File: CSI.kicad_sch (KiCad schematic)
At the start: 33 parts, among them U6 MAX9295A, Y1 Resonator_25MHz_ABM8G

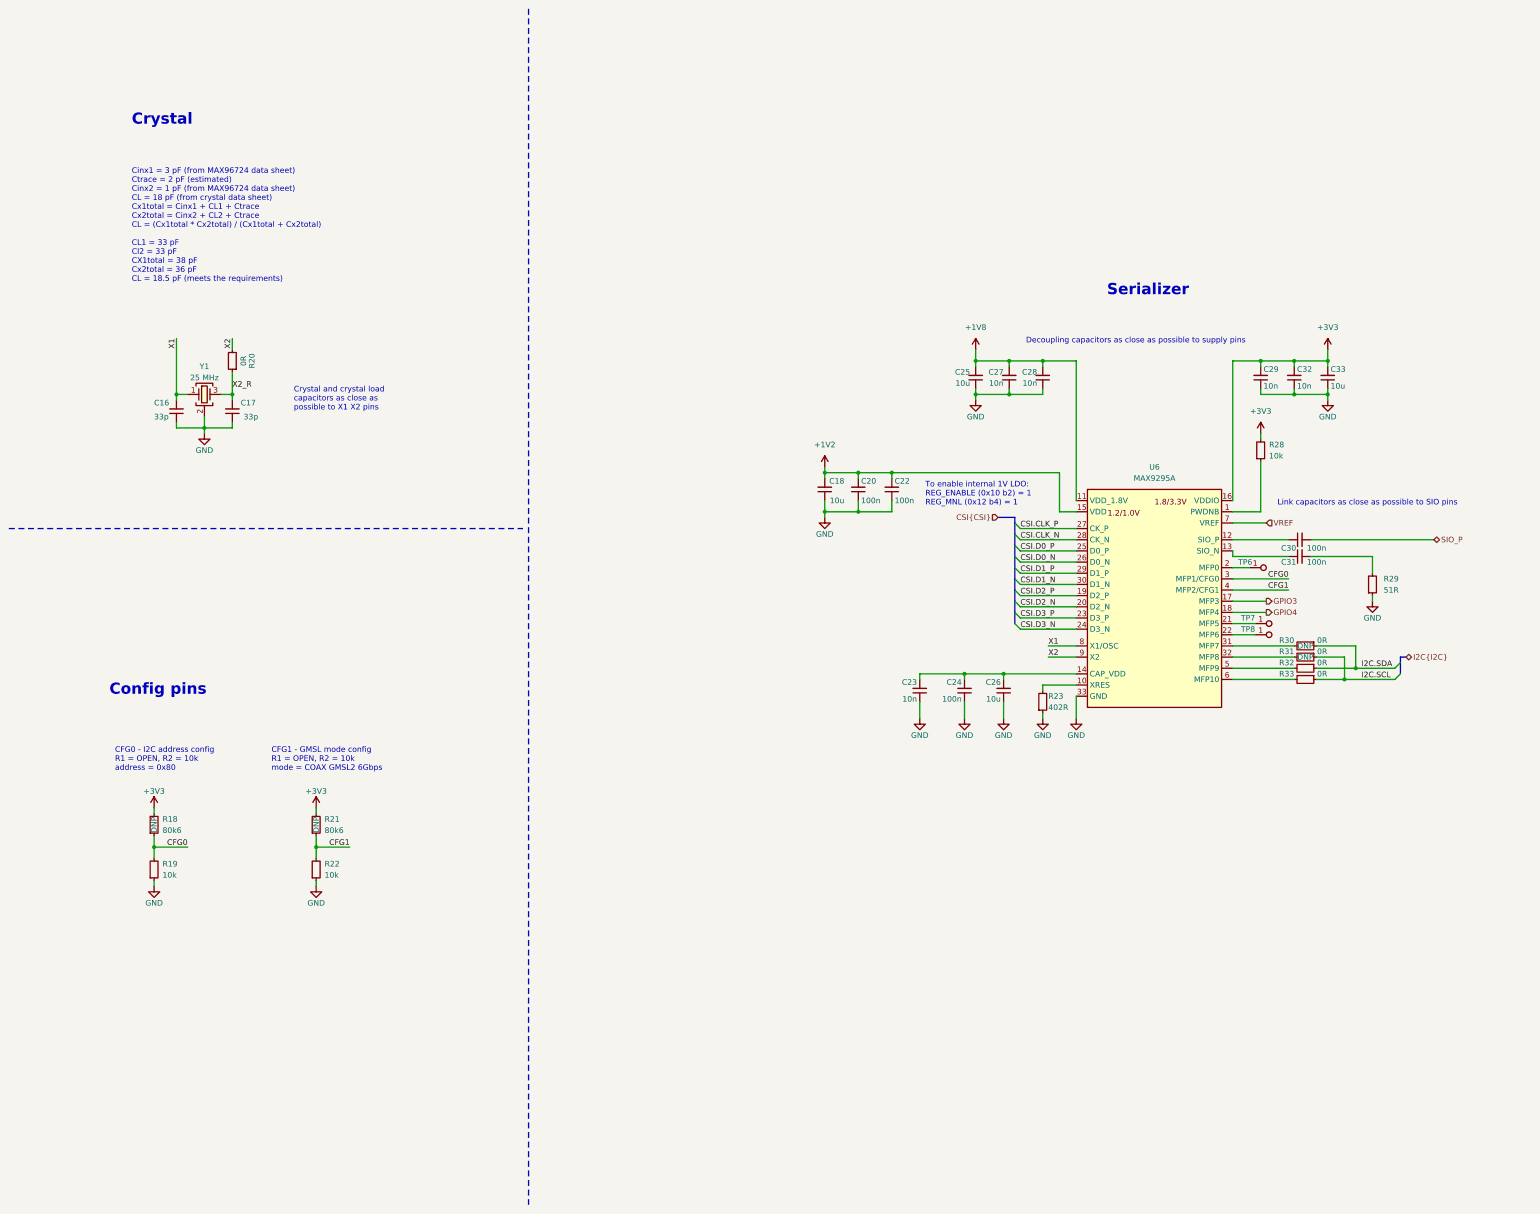
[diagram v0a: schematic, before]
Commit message: [#66847] Make schematic hierarchical
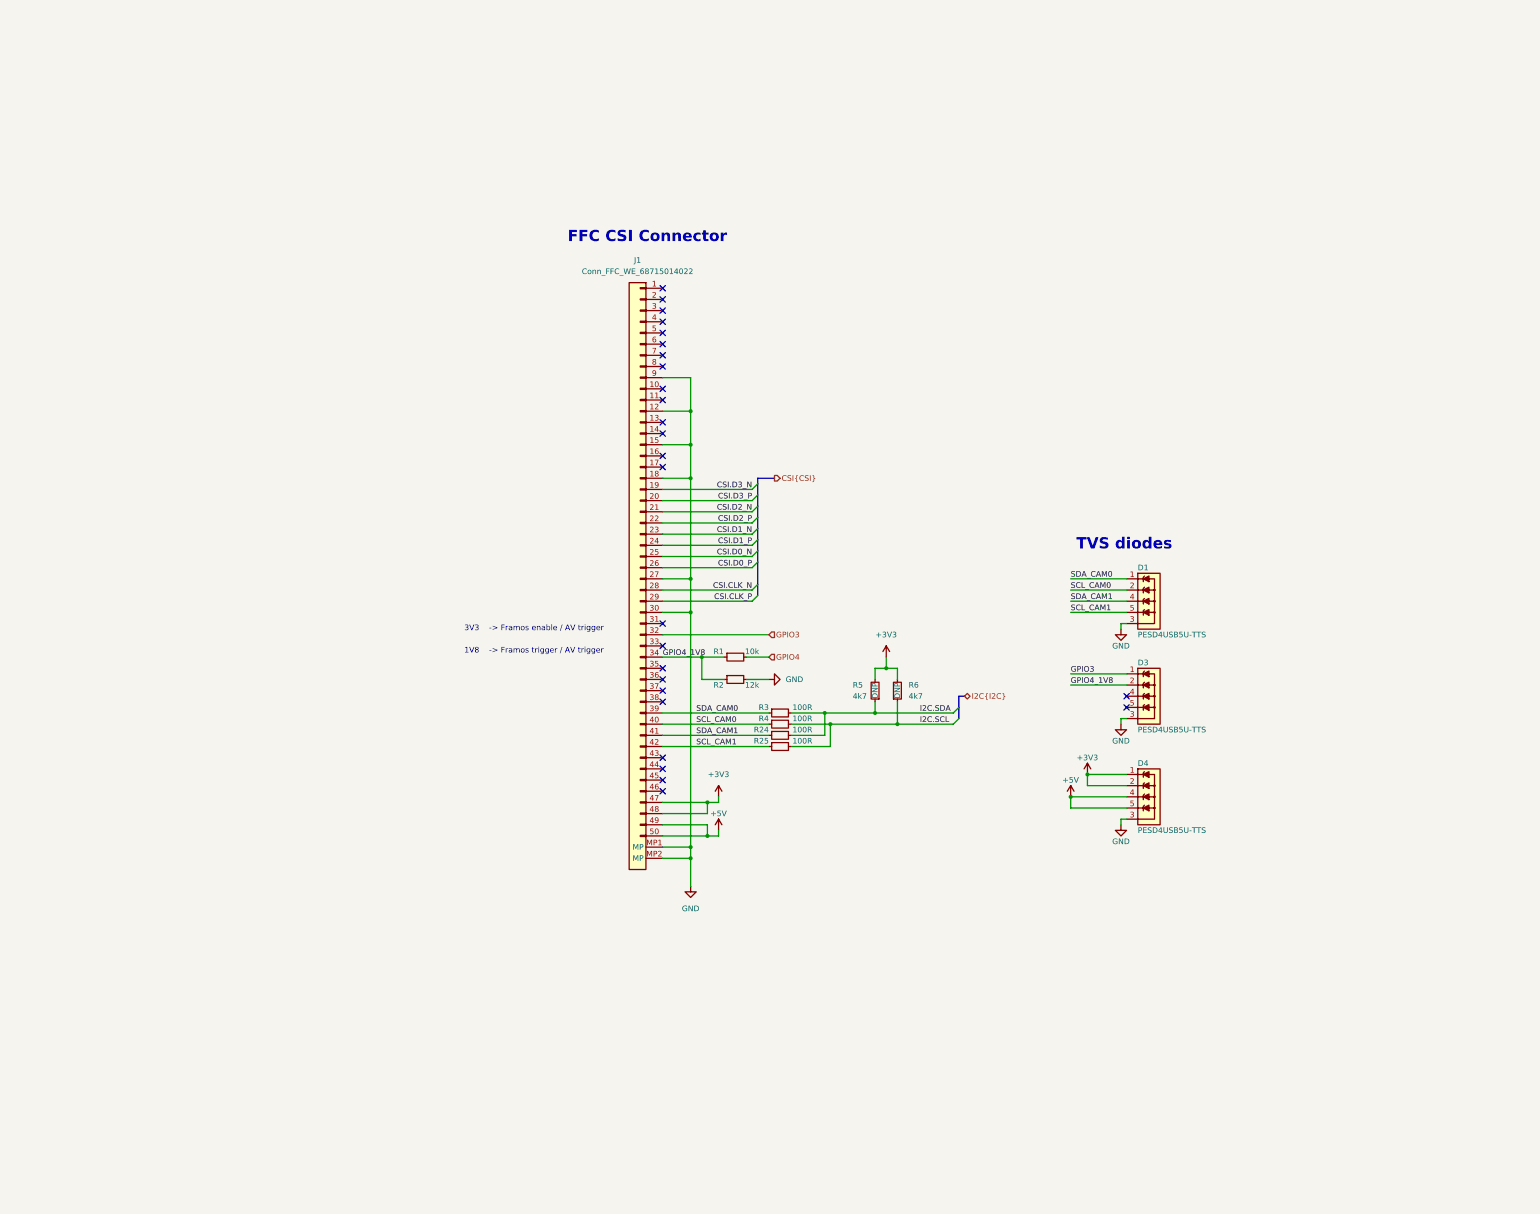
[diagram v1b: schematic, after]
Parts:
- removed C16, C17: C_33p_0402, antmicro-footprints:C_0402_1005Metric, symbol antmicroCapacitors0402:C_33p_0402
- removed C18, C25, C26, C33: C_10u_0402, antmicro-footprints:C_0402_1005Metric, symbol antmicroCapacitors0402:C_10u_0402
- removed C20, C22, C24, C30, C31: C_100n_0402, antmicro-footprints:C_0402_1005Metric, symbol antmicroCapacitors0402:C_100n_0402
- removed C23, C27, C28, C29, C32: C_10n_0402, antmicro-footprints:C_0402_1005Metric, symbol antmicroCapacitors0402:C_10n_0402
- removed R18, R21: R_80k6_0402, antmicro-footprints:R_0402_1005Metric, symbol antmicroResistors0402:R_80k6_0402
- removed R19, R22, R28: R_10k_0402, antmicro-footprints:R_0402_1005Metric, symbol antmicroResistors0402:R_10k_0402
- removed R20, R30, R31, R32, R33: R_0R_0402, antmicro-footprints:R_0402_1005Metric, symbol antmicroResistors0402:R_0R_0402
- removed R23: R_402R_0402, antmicro-footprints:R_0402_1005Metric, symbol antmicroResistors0402:R_402R_0402
- removed R29: R_51R_0402, antmicro-footprints:R_0402_1005Metric, symbol antmicroResistors0402:R_51R_0402
- removed TP6, TP7, TP8: TP_1.5mm_SMD, antmicro-footprints:TP_SMD_1.5mm, symbol antmicroTestPoints:TP_1.5mm_SMD
- removed U6: MAX9295A, antmicro-footprints:QFN-32-1EP_5x5mm, symbol antmicroInterfaceControllers:MAX9295A
- removed Y1: Resonator_25MHz_ABM8G, antmicro-footprints:Resonator_SMD_Abracon_ABM8G_3.2x2.5mm, symbol antmicroResonators:Resonator_25MHz_ABM8G
- added D1, D3, D4: PESD4USB5U-TTS, antmicro-footprints:DFN-10_2.5x1mm, symbol antmicroTVSDiodes:PESD4USB5U-TTS
- added J1: Conn_FFC_WE_68715014022, antmicro-footprints:Conn_FFC_WE_68715014x22, symbol antmicroFCCConnectors:Conn_FFC_WE_68715014022
- added R1: R_10k_0402, antmicro-footprints:R_0402_1005Metric, symbol antmicroResistors0402:R_10k_0402
- added R2: R_12k_0402, antmicro-footprints:R_0402_1005Metric, symbol antmicroResistors0402:R_12k_0402
- added R24, R25, R3, R4: R_100R_0402, antmicro-footprints:R_0402_1005Metric, symbol antmicroResistors0402:R_100R_0402
- added R5, R6: R_4k7_0402, antmicro-footprints:R_0402_1005Metric, symbol antmicroResistors0402:R_4k7_0402
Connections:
- net +3V3: now also D4.1, D4.10, D4.2, D4.9, J1.47, J1.48, R5.2, R6.2
- net CSI.CLK_N: now also J1.28
- net CSI.CLK_P: now also J1.29
- net CSI.D0_N: now also J1.25
- net CSI.D0_P: now also J1.26
- net CSI.D1_N: now also J1.23
- net CSI.D1_P: now also J1.24
- net CSI.D2_N: now also J1.21
- net CSI.D2_P: now also J1.22
- net CSI.D3_N: now also J1.19
- net CSI.D3_P: now also J1.20
- net GND: now also D1.3, D1.8, D3.3, D3.8, D4.3, D4.8, J1.12, J1.15, J1.18, J1.27, J1.30, J1.9, J1.MP1 (MP), J1.MP2 (MP), R2.2
- net GPIO3: now also D3.1, D3.10, J1.32
- net GPIO4: now also R1.2
- net I2C.SCL: now also R25.2, R4.2, R6.1
- net I2C.SDA: now also R24.2, R3.2, R5.1
- new net: D3.4, D3.7
- new net: D3.5, D3.6
- new net +5V: D4.4, D4.5, D4.6, D4.7, J1.49, J1.50
- new net GPIO4_1V8: D3.2, D3.9, J1.34, R1.1, R2.1
- new net SCL_CAM0: D1.2, D1.9, J1.40, R4.1
- new net SCL_CAM1: D1.5, D1.6, J1.42, R25.1
- new net SDA_CAM0: D1.1, D1.10, J1.39, R3.1
- new net SDA_CAM1: D1.4, D1.7, J1.41, R24.1
- no-connect marks 0 -> 26
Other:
- note added: "1V8 -> Framos trigger / AV trigger"
- note added: "3V3 -> Framos enable / AV trigger"
- note added: "FFC CSI Connector"
- note added: "TVS diodes"
- note removed: "CFG0 - I2C address config R1 = OPEN, R2 = 10k address = 0x80"
- note removed: "CFG1 - GMSL mode config R1 = OPEN, R2 = 10k mode = COAX GMSL2 6Gbps"
- note removed: "Cinx1 = 3 pF (from MAX96724 data sheet) Ctrace = 2 pF (estimated) Cinx2 = 1 pF (from MAX96724 data sheet) CL = 18 pF (from crystal data sheet) Cx1total = Cinx1 + CL1 + Ctrace Cx2total = Cinx2 + CL2 + Ctrace CL = (Cx1total * Cx2total) / (Cx1total + Cx2total) CL1 = 33 pF Cl2 = 33 pF CX1total = 38 pF Cx2total = 36 pF CL = 18.5 pF (meets the requirements)"
- note removed: "Config pins"
- note removed: "Crystal"
- note removed: "Crystal and crystal load capacitors as close as possible to X1 X2 pins"
- note removed: "Decoupling capacitors as close as possible to supply pins"
- note removed: "Link capacitors as close as possible to SIO pins"
- note removed: "Serializer"
- note removed: "To enable internal 1V LDO: REG_ENABLE (0x10 b2) = 1 REG_MNL (0x12 b4) = 1"

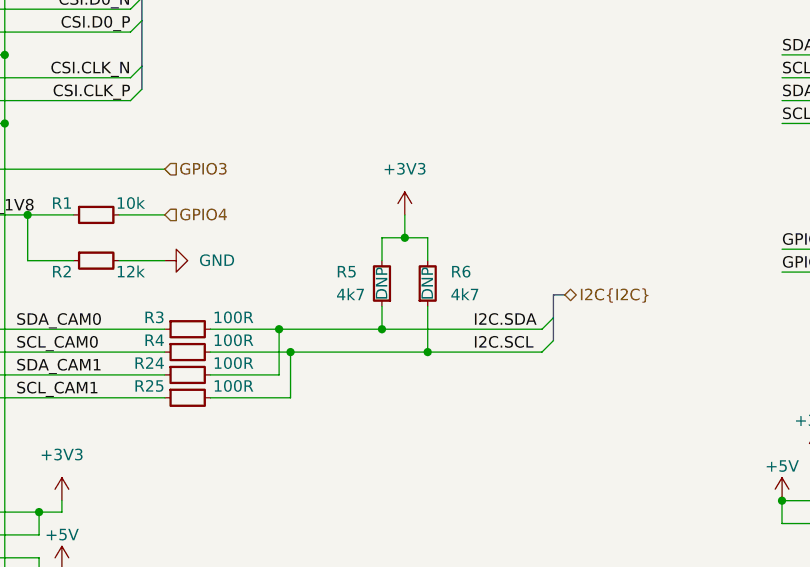
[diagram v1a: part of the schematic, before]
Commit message: [#66847] unDNP pullups on I2C; update pcb from sch
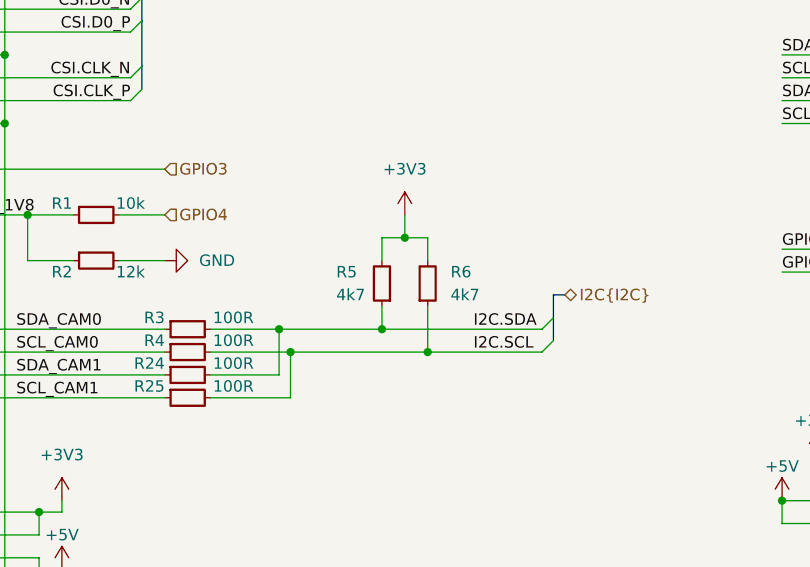
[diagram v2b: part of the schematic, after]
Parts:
- R5, R6: DNP DNP -> (none); now in the parts list
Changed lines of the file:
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@@
   )
   (symbol (lib_id "antmicroResistors0402:R_4k7_0402") (at 209.55 171.45 270) (mirror x) (unit 1)
-    (in_bom no) (on_board yes) (dnp no)
+    (in_bom yes) (on_board yes) (dnp no)
     (property "Reference" "R5" (at 204.47 167.64 90)
       (effects (font (size 1.27 1.27) (thickness 0.15)) (justify left))
@@
     (property "Tolerance" "1%" (at 199.39 151.13 0)
       (effects (font (size 1.27 1.27)) (justify left bottom) hide)
-    )
-    (property "DNP" "DNP" (at 209.55 168.91 0)
-      (effects (font (size 1.27 1.27)))
     )
     (pin "1")
@@
   )
   (symbol (lib_id "antmicroResistors0402:R_4k7_0402") (at 214.63 171.45 90) (unit 1)
-    (in_bom no) (on_board yes) (dnp no)
+    (in_bom yes) (on_board yes) (dnp no)
     (property "Reference" "R6" (at 217.17 167.6399 90)
       (effects (font (size 1.27 1.27) (thickness 0.15)) (justify right))
@@
       (effects (font (size 1.27 1.27)) (justify left bottom) hide)
     )
-    (property "DNP" "DNP" (at 214.63 168.91 0)
-      (effects (font (size 1.27 1.27)))
-    )
-    (pin "1")
+    (pin "1")

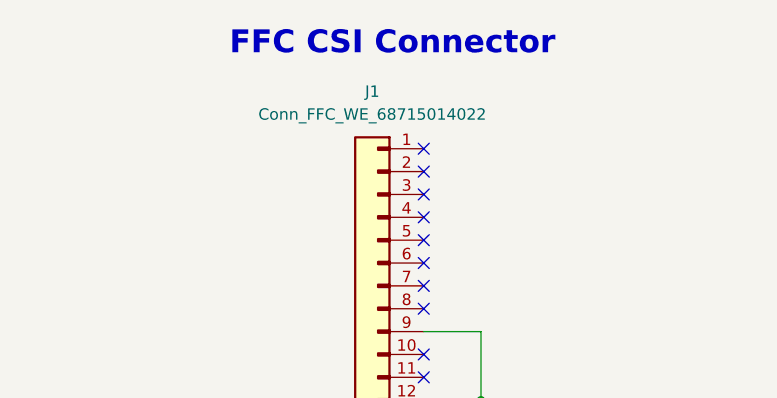
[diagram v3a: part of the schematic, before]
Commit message: [#66847] Show MPN insted value; Update description
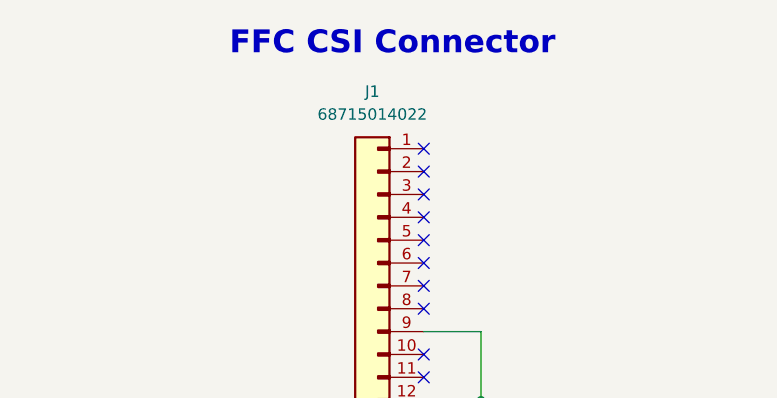
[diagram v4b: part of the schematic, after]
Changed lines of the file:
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@@
     )
     (property "Value" "Conn_FFC_WE_68715014022" (at 155.575 73.66 0)
-      (effects (font (size 1.27 1.27) (thickness 0.15)))
+      (effects (font (size 1.27 1.27) (thickness 0.15)) hide)
     )
     (property "Footprint" "antmicro-footprints:Conn_FFC_WE_68715014x22" (at 142.24 87.63 0)
@@
       (effects (font (size 1.27 1.27) (thickness 0.15)) (justify left bottom) hide)
     )
-    (property "MPN" "68715014022" (at 142.24 92.71 0)
-      (effects (font (size 1.27 1.27) (thickness 0.15)) (justify left bottom) hide)
+    (property "MPN" "68715014022" (at 155.575 73.66 0)
+      (effects (font (size 1.27 1.27) (thickness 0.15)))
     )
     (property "Manufacturer" "Würth Elektronik" (at 142.24 95.25 0)
